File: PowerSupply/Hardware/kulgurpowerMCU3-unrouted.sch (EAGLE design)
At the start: 150 parts, among them U1 MPU-6000QFN-24, U2 MPU-6000QFN-24, X1 12Mhz, X2 2534-, X3 22-23-2021

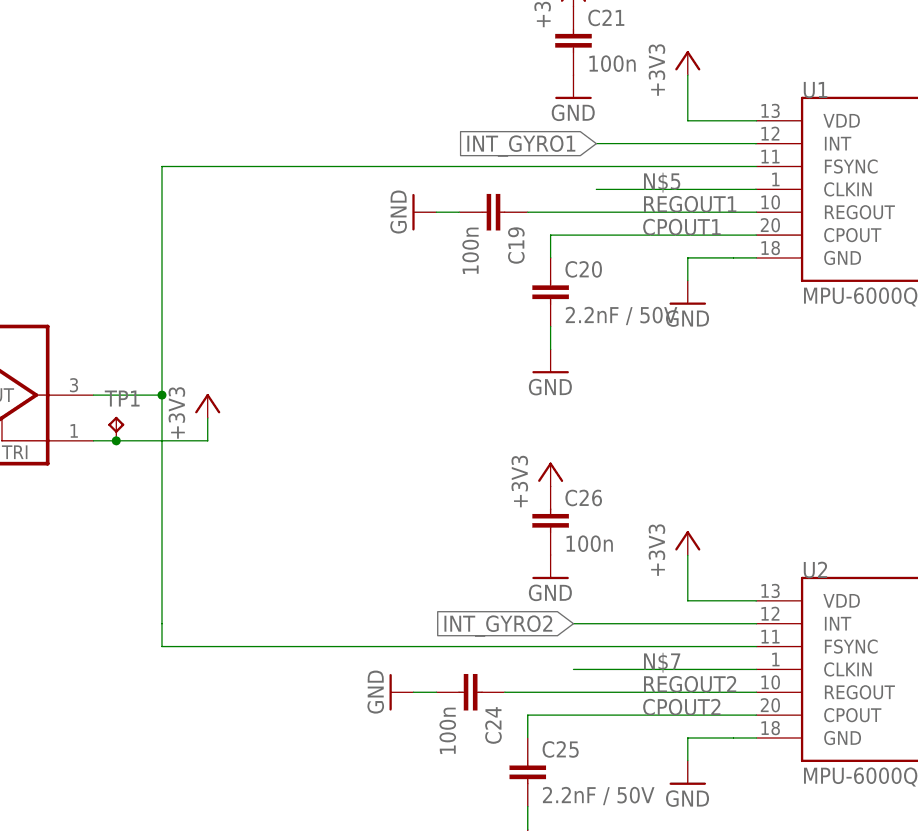
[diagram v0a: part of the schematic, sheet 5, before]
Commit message: PCB/sch small changes. 19.2Mhz fix additional transistor PSU resistor fixes
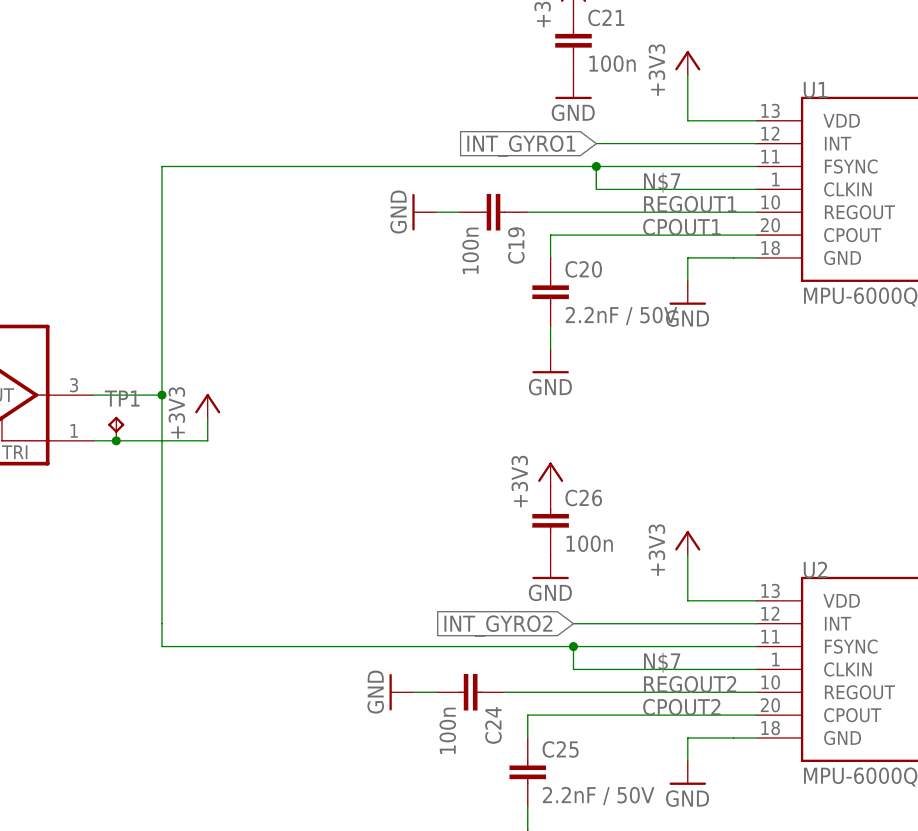
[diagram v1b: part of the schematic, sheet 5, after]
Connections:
- removed net N$26: U$4.OUT, U1.FSYNC, U2.FSYNC
- removed net N$5: U1.CLKIN
- net N$7: now also U$4.OUT, U1.CLKIN, U1.FSYNC, U2.FSYNC
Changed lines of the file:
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@@
-</segment>
-</net>
-<net name="N$5" class="0">
-<segment>
-<pinref part="U1" gate="G$1" pin="CLKIN"/>
-<wire x1="134.62" y1="119.38" x2="116.84" y2="119.38" width="0.1524" layer="91"/>
-<label x="121.92" y="119.38" size="1.778" layer="95"/>
 </segment>
 </net>
@@
 <wire x1="134.62" y1="66.04" x2="114.3" y2="66.04" width="0.1524" layer="91"/>
 <label x="121.92" y="66.04" size="1.778" layer="95"/>
-</segment>
-</net>
-<net name="N$26" class="0">
-<segment>
+<pinref part="U1" gate="G$1" pin="CLKIN"/>
+<wire x1="134.62" y1="119.38" x2="116.84" y2="119.38" width="0.1524" layer="91"/>
+<label x="121.92" y="119.38" size="1.778" layer="95"/>
 <pinref part="U1" gate="G$1" pin="FSYNC"/>
-<wire x1="134.62" y1="121.92" x2="68.58" y2="121.92" width="0.1524" layer="91"/>
+<wire x1="134.62" y1="121.92" x2="116.84" y2="121.92" width="0.1524" layer="91"/>
+<wire x1="116.84" y1="121.92" x2="68.58" y2="121.92" width="0.1524" layer="91"/>
 <wire x1="68.58" y1="121.92" x2="68.58" y2="96.52" width="0.1524" layer="91"/>
 <wire x1="68.58" y1="96.52" x2="68.58" y2="71.12" width="0.1524" layer="91"/>
 <wire x1="68.58" y1="71.12" x2="68.58" y2="68.58" width="0.1524" layer="91"/>
 <pinref part="U2" gate="G$1" pin="FSYNC"/>
-<wire x1="68.58" y1="68.58" x2="134.62" y2="68.58" width="0.1524" layer="91"/>
+<wire x1="68.58" y1="68.58" x2="114.3" y2="68.58" width="0.1524" layer="91"/>
 <pinref part="U$4" gate="G$1" pin="OUT"/>
+<wire x1="114.3" y1="68.58" x2="134.62" y2="68.58" width="0.1524" layer="91"/>
 <wire x1="60.96" y1="96.52" x2="68.58" y2="96.52" width="0.1524" layer="91"/>
 <junction x="68.58" y="96.52"/>
+<wire x1="116.84" y1="119.38" x2="116.84" y2="121.92" width="0.1524" layer="91"/>
+<wire x1="114.3" y1="66.04" x2="114.3" y2="68.58" width="0.1524" layer="91"/>
+<junction x="114.3" y="68.58"/>
+<junction x="116.84" y="121.92"/>
 </segment>
 </net>
